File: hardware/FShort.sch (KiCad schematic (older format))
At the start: 45 parts, among them J1 Conn_01x03_Male, J10 Conn_01x04_Male, J11 Conn_02x05_Odd_Even, J12 Conn_02x03_Odd_Even, J13 MicroSD, J14 Conn_01x01_Male, J2 Conn_01x07_Female, J3 Conn_01x03_Male, J4 Conn_01x03_Male, J5 USB_B_Micro, J6 Conn_02x05_Odd_Even, J7 Conn_01x04_Male, J8 Conn_01x04_Male, J9 Conn_01x04_Male, SW1 SW_Push, U1 STM32F103RETx, U2 SN74LVC1T45DBV, U3 SN74LVC1T45DBV, U4 AP7365-SOT25, U5 W25Q64JV, U6 E19-868M30S, Y1 8Mhz, Y2 32.768KHz

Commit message: New version of PCB, several bugs fixed
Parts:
- removed J14: Conn_01x01_Male, Connector_Wire:SolderWirePad_1x01_SMD_5x10mm, symbol Connector:Conn_01x01_Male
- removed U6: E19-868M30S, Personal:E19-868MS1W, symbol Personal:E19-868M30S
- added AE1: Antenna_Shield, Personal:KH-IPEX3-2020, symbol Device:Antenna_Shield
- added C15, C16: 3n3, Capacitor_SMD:C_0603_1608Metric, symbol Device:C
- added D2, D3: ZMM7V5, Diode_SMD:D_MiniMELF, symbol Diode:ZMMxx
- added E1, E2: SPARK_GAP, Personal:SDI12-SparkGap, symbol Device:SPARK_GAP
- added R10, R12, R7, R9: 510, Resistor_SMD:R_0603_1608Metric, symbol Device:R
- added R11, R8: 200k, Resistor_SMD:R_0603_1608Metric, symbol Device:R
- added U6: E19-868M30S_Vollgo, Personal:E19-868MS1W_VollGo, symbol Personal:E19-868M30S_Vollgo
- U5: footprint Package_SO:SOP-8_3.9x4.9mm_P1.27mm -> Package_SO:SOP-8_5.28x5.23mm_P1.27mm
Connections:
- net +3V3: now also U6.23 (3V3)
- net +5V: now also U6.11 (VCC)
- net GND: now also AE1.2 (Shield), C15.2, C16.2, D2.2 (A), D3.2 (A), E1.2, E2.2, R11.1, R8.1, U6.1 (GND), U6.10 (GND), U6.18 (GND), U6.20 (GND), U6.21 (GND), U6.22 (GND), U6.9 (GND)
- net RADIO_NSS: now also U6.15 (~SS)
- net Radio_dio0: now also U6.7 (DIO0)
- net Radio_dio1: now also U6.6 (DIO1)
- net Radio_rst: now also U6.8 (RST)
- net Radio_rxen: now also U6.17 (RXEN)
- net Radio_txen: now also U6.16 (TXEN)
- net SPI1_MISO: now also U6.13 (MISO)
- net SPI1_MOSI: now also U6.14 (MOSI)
- net SPI1_SCK: now also U6.12 (SCK)
- net at U2.3 (A): now also R10.2; no longer J3.2 (Pin_2)
- net at U3.3 (A): now also R12.1; no longer J4.2 (Pin_2)
- new net: E2.1, J4.2 (Pin_2), R9.2
- new net: E1.1, J3.2 (Pin_2), R7.1
- new net: AE1.1 (A), U6.24 (RF)
- new net: C15.1, D2.1 (K), R10.1, R7.2, R8.2
- new net: C16.1, D3.1 (K), R11.2, R12.2, R9.1
- no-connect marks 11 -> 12
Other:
- moved on the sheet: J10, J3, J4, R4, R6, U2, U3, U5

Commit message: New PCB, some minor fixes
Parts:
- C3, C4: value 20p -> 15p
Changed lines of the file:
@@
 P 1250 5050
 F 0 "C3" V 1021 5050 50  0000 C CNN
-F 1 "20p" V 1112 5050 50  0000 C CNN
+F 1 "15p" V 1112 5050 50  0000 C CNN
 F 2 "Capacitor_SMD:C_0603_1608Metric" H 1250 5050 50  0001 C CNN
 F 3 "~" H 1250 5050 50  0001 C CNN
@@
 P 1250 5450
 F 0 "C4" V 1021 5450 50  0000 C CNN
-F 1 "20p" V 1112 5450 50  0000 C CNN
+F 1 "15p" V 1112 5450 50  0000 C CNN
 F 2 "Capacitor_SMD:C_0603_1608Metric" H 1250 5450 50  0001 C CNN
 F 3 "~" H 1250 5450 50  0001 C CNN

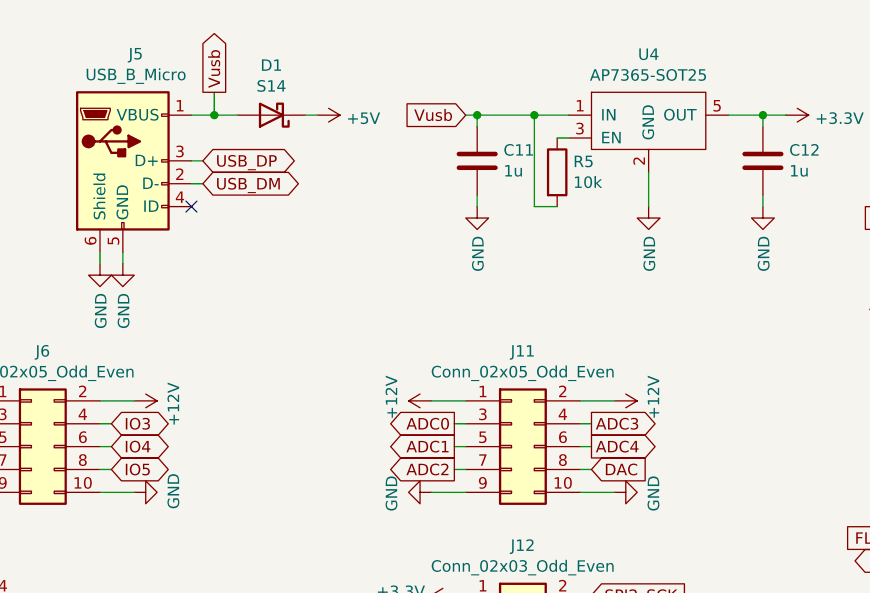
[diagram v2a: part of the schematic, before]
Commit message: Added USB support Added Port and Socket abstraction classes Added simple HTTP support through GSM Added a kernel level message queue
KVS module setting system
LoRa variable refactoring
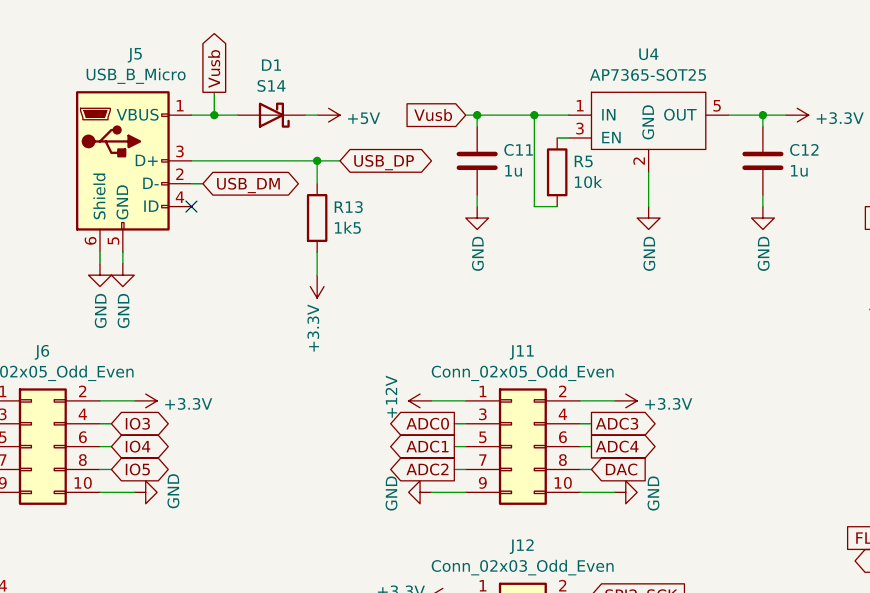
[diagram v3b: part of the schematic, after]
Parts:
- added R13: 1k5, Resistor_SMD:R_0603_1608Metric, symbol Device:R
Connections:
- net +12V: no longer J11.2 (Pin_2), J6.2 (Pin_2)
- net +3V3: now also J11.2 (Pin_2), J6.2 (Pin_2), R13.2
- net USB_DP: now also R13.1
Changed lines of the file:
@@
-$EndComp
-$Comp
-L power:+12V #PWR033
-U 1 1 5EFBC514
-P 5600 2100
-F 0 "#PWR033" H 5600 1950 50  0001 C CNN
-F 1 "+12V" H 5615 2273 50  0000 C CNN
-F 2 "" H 5600 2100 50  0001 C CNN
-F 3 "" H 5600 2100 50  0001 C CNN
-	1    5600 2100
-	0    1    1    0
 $EndComp
 $Comp
@@
 Wire Wire Line
 	4950 2500 4800 2500
-Wire Wire Line
-	5600 2100 5450 2100
 Wire Wire Line
 	5600 2500 5450 2500
@@
 Text GLabel 5900 1150 2    50   BiDi ~ 0
 USB_DM
-Text GLabel 5900 1050 2    50   BiDi ~ 0
+Text GLabel 6500 1050 2    50   BiDi ~ 0
 USB_DP
 Wire Wire Line
-	5900 1050 5850 1050
+	6500 1050 6400 1050
 $Comp
 L Connector:USB_B_Micro J5
@@
 	1    6900 2500
 	0    1    1    0
-$EndComp
-$Comp
-L power:+12V #PWR052
-U 1 1 5F76EE99
-P 7700 2100
-F 0 "#PWR052" H 7700 1950 50  0001 C CNN
-F 1 "+12V" H 7715 2273 50  0000 C CNN
-F 2 "" H 7700 2100 50  0001 C CNN
-F 3 "" H 7700 2100 50  0001 C CNN
-	1    7700 2100
-	0    1    -1   0
 $EndComp
 $Comp
@@
 	10450 4600 10500 4600
 NoConn ~ 10150 5200
+$Comp
+L Device:R R13
+U 1 1 5F83FA06
+P 6400 1300
+F 0 "R13" H 6470 1346 50  0000 L CNN
+F 1 "1k5" H 6470 1255 50  0000 L CNN
+F 2 "Resistor_SMD:R_0603_1608Metric" V 6330 1300 50  0001 C CNN
+F 3 "~" H 6400 1300 50  0001 C CNN
+	1    6400 1300
+	1    0    0    -1
+$EndComp
+Wire Wire Line
+	6400 1150 6400 1050
+Connection ~ 6400 1050
+Wire Wire Line
+	6400 1050 5850 1050
+$Comp
+L power:+3.3V #PWR0103
+U 1 1 5F859748
+P 6400 1550
+F 0 "#PWR0103" H 6400 1400 50  0001 C CNN
+F 1 "+3.3V" V 6415 1678 50  0000 L CNN
+F 2 "" H 6400 1550 50  0001 C CNN
+F 3 "" H 6400 1550 50  0001 C CNN
+	1    6400 1550
+	-1   0    0    1
+$EndComp
+Wire Wire Line
+	6400 1550 6400 1450
+Wire Wire Line
+	5600 2100 5450 2100
+$Comp
+L power:+3.3V #PWR?
+U 1 1 5F889A10
+P 5600 2100
+F 0 "#PWR?" H 5600 1950 50  0001 C CNN
+F 1 "+3.3V" V 5615 2228 50  0000 L CNN
+F 2 "" H 5600 2100 50  0001 C CNN
+F 3 "" H 5600 2100 50  0001 C CNN
+	1    5600 2100
+	0    1    1    0
+$EndComp
+$Comp
+L power:+3.3V #PWR?
+U 1 1 5F889DFB
+P 7700 2100
+F 0 "#PWR?" H 7700 1950 50  0001 C CNN
+F 1 "+3.3V" V 7715 2228 50  0000 L CNN
+F 2 "" H 7700 2100 50  0001 C CNN
+F 3 "" H 7700 2100 50  0001 C CNN
+	1    7700 2100
+	0    1    1    0
+$EndComp
 $EndSCHEMATC
